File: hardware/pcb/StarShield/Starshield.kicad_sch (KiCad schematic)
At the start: 0 parts

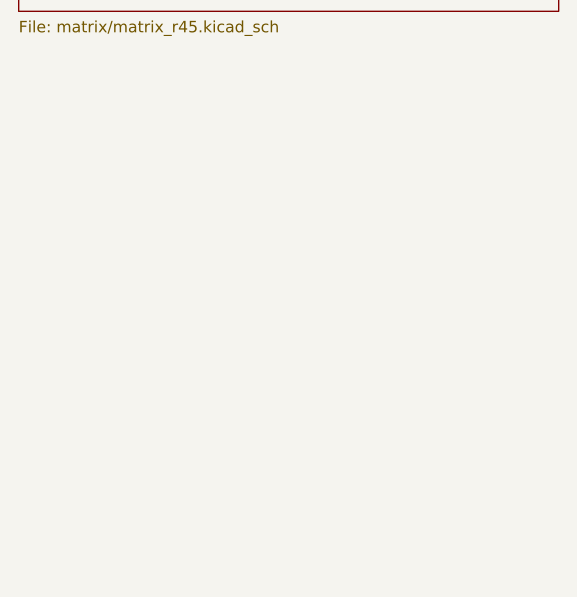
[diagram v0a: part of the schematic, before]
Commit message: feat(power): 电源子图（BQ24072 电源路径 + 拓扑 C 门控），ERC 0 error
产物 hardware/pcb/StarShield/power/power.kicad_sch：18 元件 —— USB-C 输入+CC 下拉、BQ24072 充电与电源路径、电池座、充电指示、2N7002+AO3401A 门控。ERC 0 error / 2 warning（warning 是待 B2 接线的跨图标签 VLED 与 RGB_PWR_EN）。

取值依据 TI SLUS810N 正文（本地抽 PDF 核对）：R_ISET=1.78k -> 0.5A；EN2=GND/EN1=OUT -> USB500 档（EN1 不能接 VBUS，该脚绝对最大额定仅 7V）；~CE 与 TD 接 VSS；TMR 悬空；TS 经 10k 到 VSS 禁用温测。定稿表见 docs/power-architecture.md 3.1。

画法：每引脚一根 2.54mm 短线 + 同名标签（连通性由网名决定，几何错误不再等于电气错误）；引脚坐标由符号定义算出。符号定义缓存在 docs/_tools/power_symbols.json（入库数据源，来源 KiCad 官方库）。

根图拆出：gen_matrix_sch.py 不再写 Starshield.kicad_sch，改由新的 gen_root_sch.py 独占（根图是工程级清单，新增子图只改一处）。矩阵三张图 UUID 未变。

校验：新增 verify_power.py（网表派生断言 + 安全关键具名断言 + ERC 零 error 闸门）。连同 check_repo_tree / verify_netlist / verify_firmware 四个校验器全绿；连跑两轮生成器后 git status 与 git diff 哈希一致。
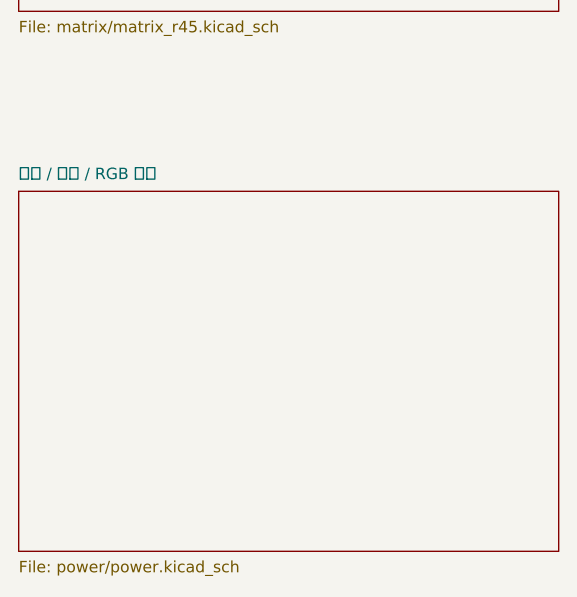
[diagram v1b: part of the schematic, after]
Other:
- added sheet 电源 / 充电 / RGB 门控 (power/power.kicad_sch)
- title: StarShield 95键矩阵（根图） -> StarShield（根图）
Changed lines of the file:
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@@
 	(generator "eeschema")
 	(generator_version "10.0")
-	(paper "A4")
+	(paper "A3")
 	(title_block
-		(title "StarShield 95键矩阵（根图）")
+		(title "StarShield（根图）")
 		(rev "0.1")
-		(comment 1 "自动生成：docs/_tools/gen_matrix_sch.py")
+		(comment 1 "自动生成：docs/_tools/gen_root_sch.py —— 新增子图只改这个文件")
 	)
 	(sheet (at 60.00 60.00) (size 60.00 40.00) (fields_autoplaced yes)
@@
 			(effects (font (size 1.27 1.27)) (justify left top)))
 	)
+	(sheet (at 60.00 240.00) (size 60.00 40.00) (fields_autoplaced yes)
+		(stroke (width 0.1524) (type solid)) (fill (color 0 0 0 0.0000))
+		(property "Sheetname" "电源 / 充电 / RGB 门控" (at 60.00 238.80 0)
+			(effects (font (size 1.27 1.27)) (justify left bottom)))
+		(property "Sheetfile" "power/power.kicad_sch" (at 60.00 281.00 0)
+			(effects (font (size 1.27 1.27)) (justify left top)))
+	)

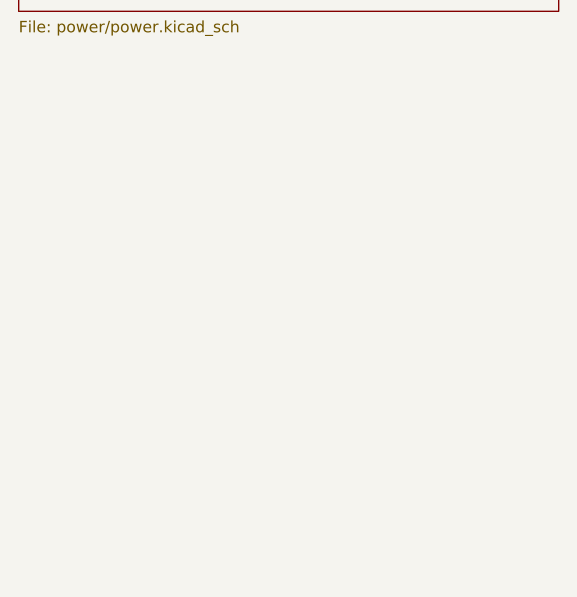
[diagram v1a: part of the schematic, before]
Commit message: feat(schematic): B2 控制板子图 —— nice!nano 排针 / 595 列驱动 / 三档开关
新增第 5 张子图 control/control.kicad_sch（9 元件 / 82 条引脚连接）：
- J3A/J3B：nice!nano v2 排针 = 两条 Conn_01x12（官方库无 Pro_Micro 符号；
  引脚号 1..12 直接对应 Pro Micro 标号 n / 12+n，映射依据 ZMK v0.3
  arduino_pro_micro_pins.dtsi）。RAW(PM13) 接电源子图 OUT，VCC(PM16) 为 3.3V 轨。
- U2/U3/U4：3 颗 74HC595 级联驱动 COL0..17（位序 bit0..7/8..15/16..17，
  已按 gpio_595.c 源码核实）；~SRCLR 接 VCC、~OE 接 GND；每颗 100nF 去耦。
- SW1：SP3T PCM13（Switch:SW_SP3T，pin3=公共端接 GND），
  三档触点接 MODE0/1/2 = D2(P0.17)/D14(P1.11)/D18(P1.15)（B2 定案）。
- 全局标签与电源/矩阵子图同名相连：OUT/RGB_PWR_EN/ROW0..5/COL0..17/LED_DIN。
- verify_control.py：派生断言 + 跨图接口断言（根图整体网表）+ 具名断言 + ERC 0 error 闸门。
- power_symbols.json 扩充为全工程符号缓存（+4 符号：74HC595/SW_SP3T/Conn_01x12/VCC）。
跨图连通已实测：COL0 含 U2+6 二极管、RGB_PWR_EN 含 J3B+R8。
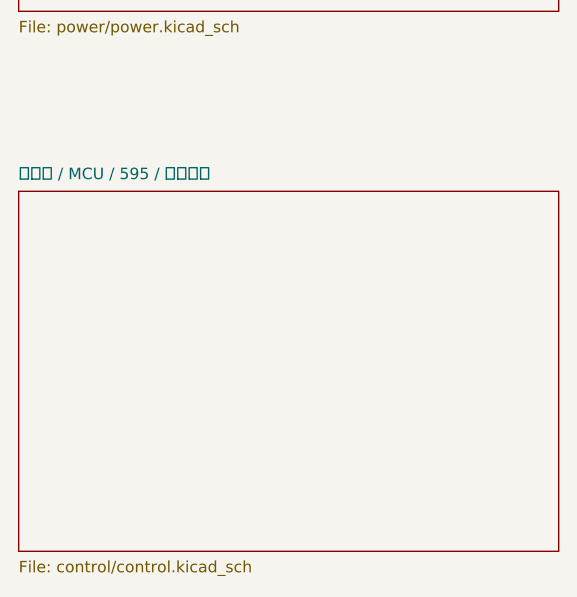
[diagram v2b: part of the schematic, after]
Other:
- added sheet 控制板 / MCU / 595 / 模式开关 (control/control.kicad_sch)
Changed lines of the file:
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@@
+			(effects (font (size 1.27 1.27)) (justify left top)))
+	)
+	(sheet (at 60.00 300.00) (size 60.00 40.00) (fields_autoplaced yes)
+		(stroke (width 0.1524) (type solid)) (fill (color 0 0 0 0.0000))
+		(property "Sheetname" "控制板 / MCU / 595 / 模式开关" (at 60.00 298.80 0)
+			(effects (font (size 1.27 1.27)) (justify left bottom)))
+		(property "Sheetfile" "control/control.kicad_sch" (at 60.00 341.00 0)
 			(effects (font (size 1.27 1.27)) (justify left top)))
 	)

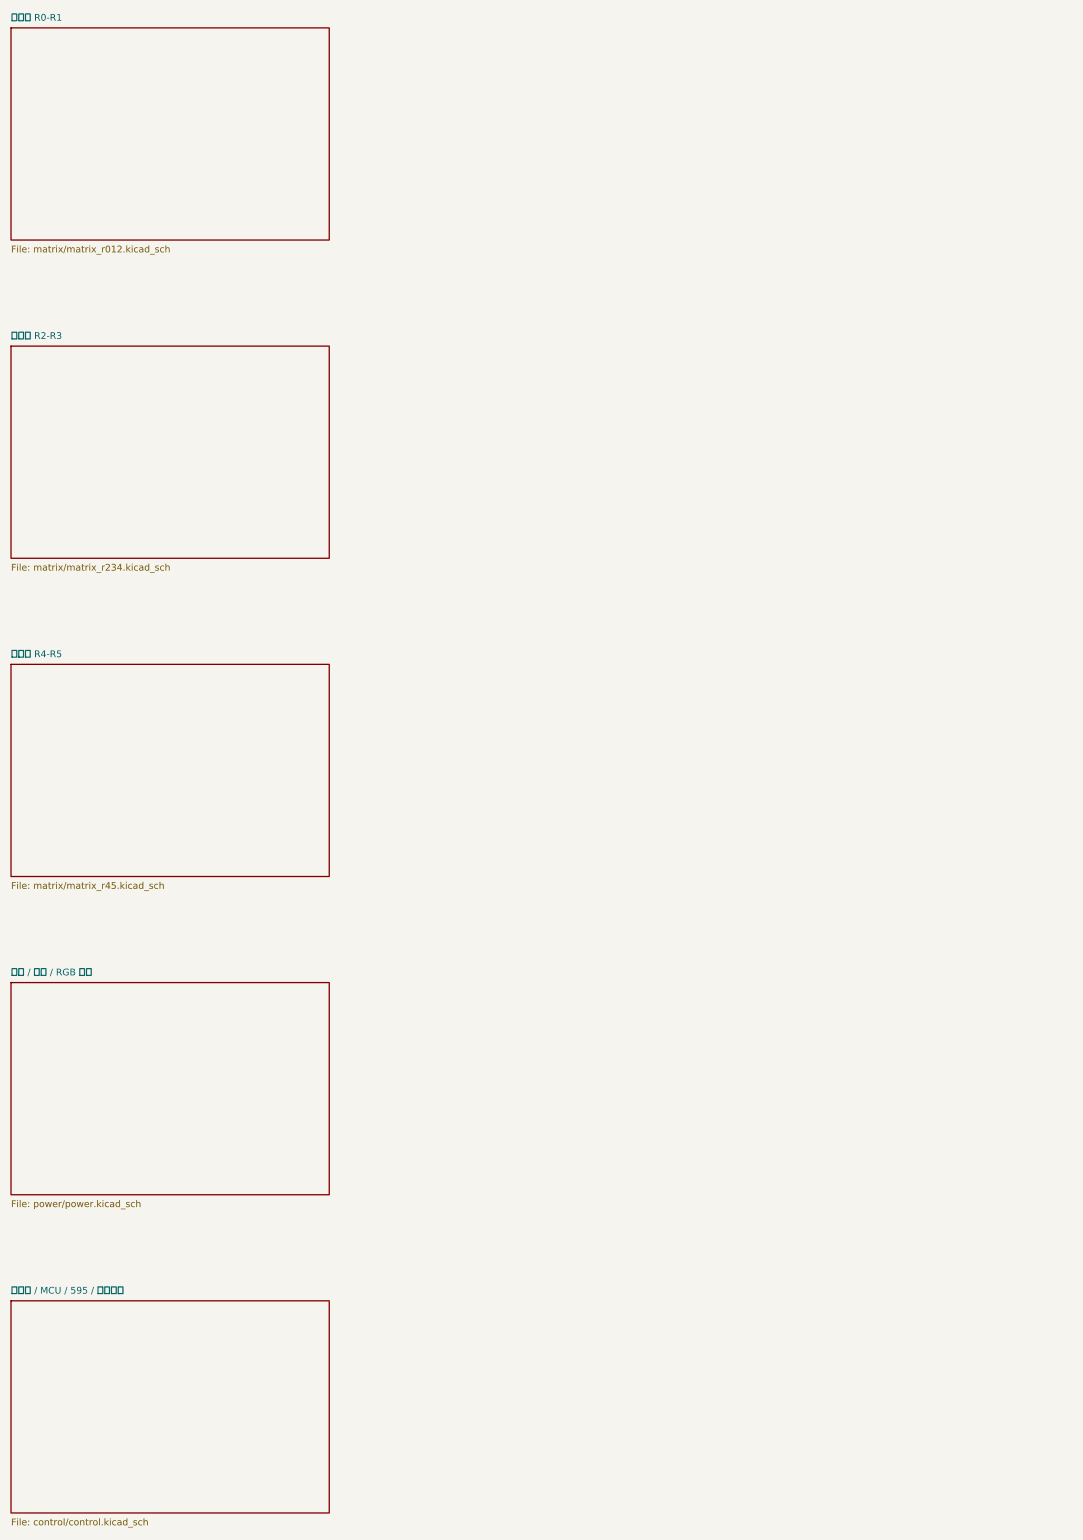
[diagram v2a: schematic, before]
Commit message: feat(schematic): M5 RGB 子图 —— 95 颗 SK6812MINI-E 数据链，原理图四张子图齐
新增第 6 张子图 rgb/rgb.kicad_sch（A2；95 灯珠 / 380 条引脚连接）：
- 数据源 rgb_design.py 由 docs/_generated/matrix.json 循环生成（位号 LED1..95 ↔ 键 index），
  链序 = 键位 index 顺序（行优先、行内从左到右），与 ZMK 侧 LED index 一致。
- LED1.DIN ← 全局 LED_DIN（控制子图 J3A.1 = P0.06 / spi3 MOSI）；LED95.DOUT 链尾 NC。
- 供电：全部 VDD → 全局 VLED（电源子图 Q1 门控的电池直供轨）；VSS → GND。
- 符号用官方 LED:SK6812MINI-E（派生符号已展平）；封装选 PLCC4 3.5x3.5 正装，
  型号-封装对应与贴装方向标 UNVERIFIED（B3/B4 用实物核对）。
- 根图改 3 列 x 2 行布局以容纳 6 张子图。
- verify_rgb.py：派生 / 跨图接口 / 具名（链序、链尾、供电）/ ERC 四组断言。

ERC：根图整体 0 error，isolated 两条（VLED / LED_DIN）就此归零。
同步：控制子图与 RGB 子图移除重复的 GND PWR_FLAG（全局网只能有一个 power output，
否则触发 ERC pin_to_pin error），改由电源子图统一提供；verify_control 断言同步。
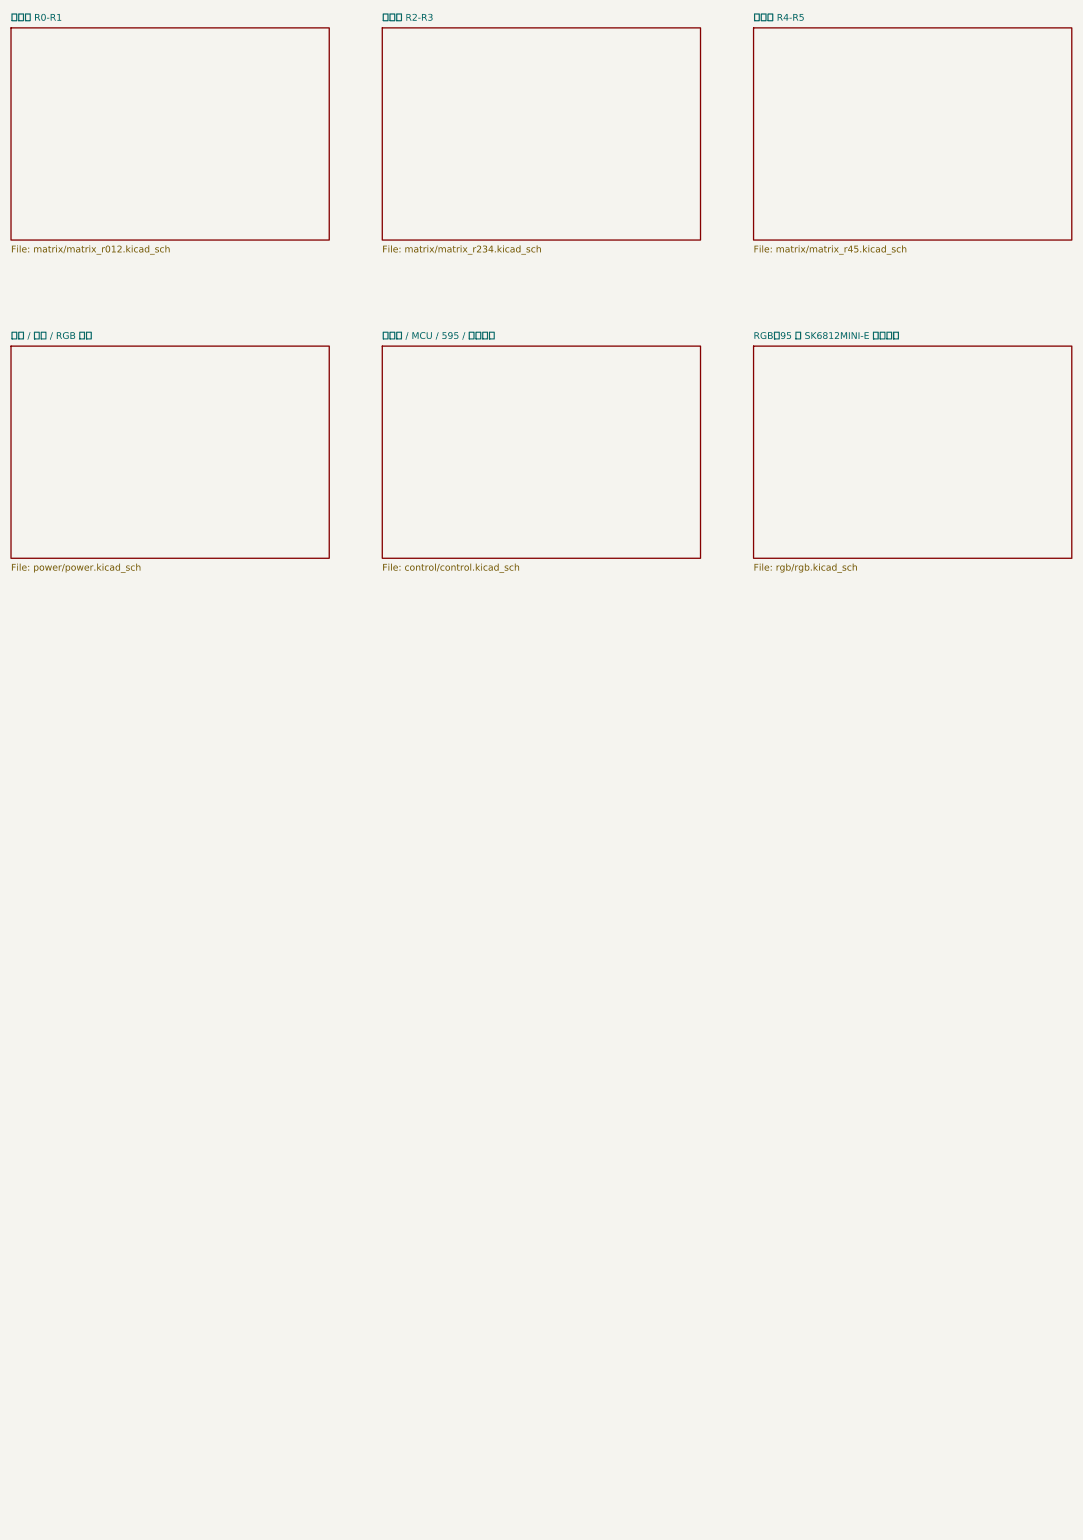
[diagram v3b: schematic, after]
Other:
- added sheet RGB（95 颗 SK6812MINI-E 数据链） (rgb/rgb.kicad_sch)
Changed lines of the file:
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@@
+			(effects (font (size 1.27 1.27)) (justify left top)))
+	)
+	(sheet (at 130.00 60.00) (size 60.00 40.00) (fields_autoplaced yes)
+		(stroke (width 0.1524) (type solid)) (fill (color 0 0 0 0.0000))
+		(property "Sheetname" "矩阵行 R2-R3" (at 130.00 58.80 0)
+			(effects (font (size 1.27 1.27)) (justify left bottom)))
+		(property "Sheetfile" "matrix/matrix_r234.kicad_sch" (at 130.00 101.00 0)
+			(effects (font (size 1.27 1.27)) (justify left top)))
+	)
+	(sheet (at 200.00 60.00) (size 60.00 40.00) (fields_autoplaced yes)
+		(stroke (width 0.1524) (type solid)) (fill (color 0 0 0 0.0000))
+		(property "Sheetname" "矩阵行 R4-R5" (at 200.00 58.80 0)
+			(effects (font (size 1.27 1.27)) (justify left bottom)))
+		(property "Sheetfile" "matrix/matrix_r45.kicad_sch" (at 200.00 101.00 0)
 			(effects (font (size 1.27 1.27)) (justify left top)))
 	)
 	(sheet (at 60.00 120.00) (size 60.00 40.00) (fields_autoplaced yes)
 		(stroke (width 0.1524) (type solid)) (fill (color 0 0 0 0.0000))
-		(property "Sheetname" "矩阵行 R2-R3" (at 60.00 118.80 0)
+		(property "Sheetname" "电源 / 充电 / RGB 门控" (at 60.00 118.80 0)
 			(effects (font (size 1.27 1.27)) (justify left bottom)))
-		(property "Sheetfile" "matrix/matrix_r234.kicad_sch" (at 60.00 161.00 0)
+		(property "Sheetfile" "power/power.kicad_sch" (at 60.00 161.00 0)
 			(effects (font (size 1.27 1.27)) (justify left top)))
 	)
-	(sheet (at 60.00 180.00) (size 60.00 40.00) (fields_autoplaced yes)
+	(sheet (at 130.00 120.00) (size 60.00 40.00) (fields_autoplaced yes)
 		(stroke (width 0.1524) (type solid)) (fill (color 0 0 0 0.0000))
-		(property "Sheetname" "矩阵行 R4-R5" (at 60.00 178.80 0)
+		(property "Sheetname" "控制板 / MCU / 595 / 模式开关" (at 130.00 118.80 0)
 			(effects (font (size 1.27 1.27)) (justify left bottom)))
-		(property "Sheetfile" "matrix/matrix_r45.kicad_sch" (at 60.00 221.00 0)
+		(property "Sheetfile" "control/control.kicad_sch" (at 130.00 161.00 0)
 			(effects (font (size 1.27 1.27)) (justify left top)))
 	)
-	(sheet (at 60.00 240.00) (size 60.00 40.00) (fields_autoplaced yes)
+	(sheet (at 200.00 120.00) (size 60.00 40.00) (fields_autoplaced yes)
 		(stroke (width 0.1524) (type solid)) (fill (color 0 0 0 0.0000))
-		(property "Sheetname" "电源 / 充电 / RGB 门控" (at 60.00 238.80 0)
+		(property "Sheetname" "RGB（95 颗 SK6812MINI-E 数据链）" (at 200.00 118.80 0)
 			(effects (font (size 1.27 1.27)) (justify left bottom)))
-		(property "Sheetfile" "power/power.kicad_sch" (at 60.00 281.00 0)
+		(property "Sheetfile" "rgb/rgb.kicad_sch" (at 200.00 161.00 0)
 			(effects (font (size 1.27 1.27)) (justify left top)))
 	)
-	(sheet (at 60.00 300.00) (size 60.00 40.00) (fields_autoplaced yes)
-		(stroke (width 0.1524) (type solid)) (fill (color 0 0 0 0.0000))
-		(property "Sheetname" "控制板 / MCU / 595 / 模式开关" (at 60.00 298.80 0)
-			(effects (font (size 1.27 1.27)) (justify left bottom)))
-		(property "Sheetfile" "control/control.kicad_sch" (at 60.00 341.00 0)
-			(effects (font (size 1.27 1.27)) (justify left top)))
-	)
